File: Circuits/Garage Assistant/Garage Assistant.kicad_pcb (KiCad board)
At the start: 2 copper layers, 80.8 x 56.9 mm, 45 parts, among them P1 MOTION_A, P2 MOTION_B, P3 AC_IN, P4 3.5mm_11pin, P5 OUT_A, P6 OUT_B, Q1 TIP122, Q2 TIP122, U1 HiLink_5V3W

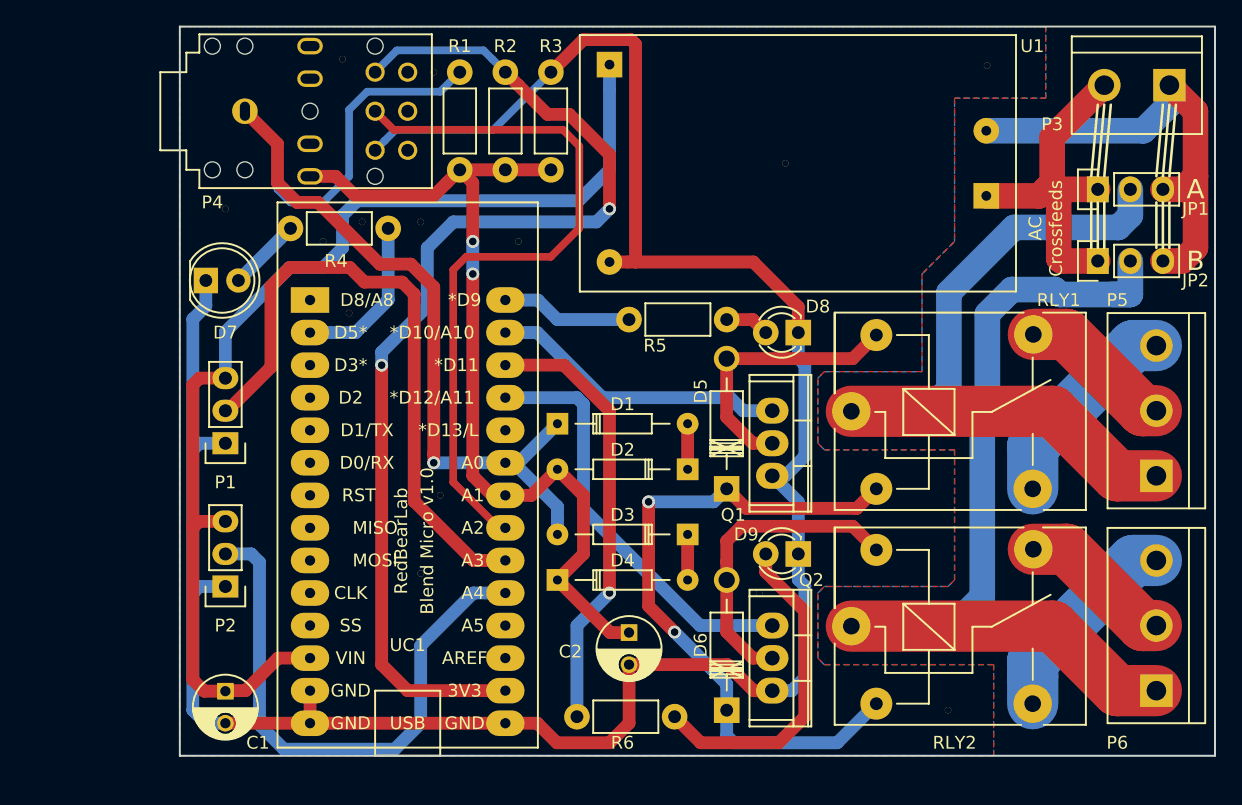
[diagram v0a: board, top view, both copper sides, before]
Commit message: Circuits: Updated 3d models on Garage Assistant
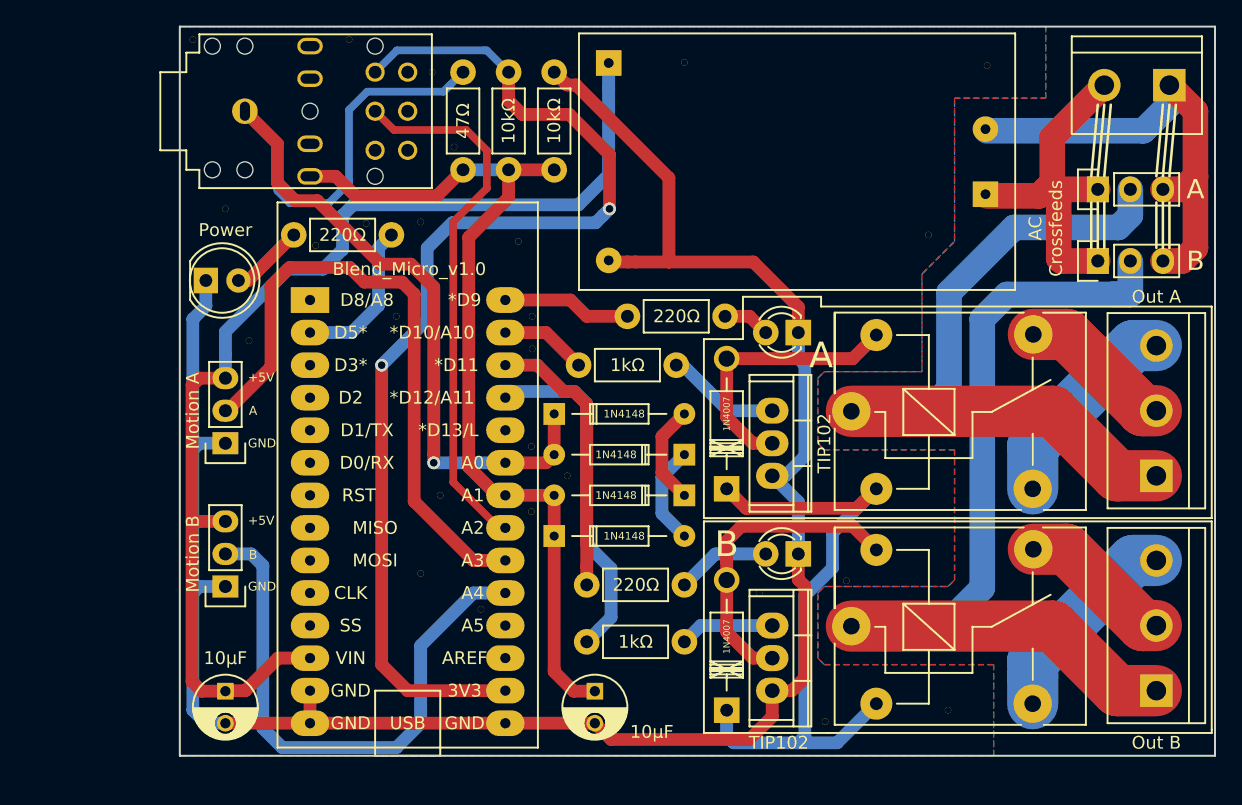
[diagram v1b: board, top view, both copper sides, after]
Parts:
- added ?: , Footprints:Thermal_Via_NoRing, F.Cu at (115.6, 89.5)
- added ?: , Footprints:Thermal_Via_NoRing, F.Cu at (111.3, 66.0)
- added ?: , Footprints:Thermal_Via_NoRing, F.Cu at (168.7, 81.3)
- added ?: , Footprints:Thermal_Via_NoRing, F.Cu at (137.7, 97.8)
- added ?: , Footprints:Thermal_Via_NoRing, F.Cu at (140.5, 100.1)
- added ?: , Footprints:Thermal_Via_NoRing, F.Cu at (131.6, 74.4)
- added ?: , Footprints:Thermal_Via_NoRing, F.Cu at (127.1, 87.6)
- added ?: , Footprints:Thermal_Via_NoRing, F.Cu at (120.8, 82.1)
- added ?: , Footprints:Thermal_Via_NoRing, F.Cu at (137.7, 102.9)
- added ?: , Footprints:Thermal_Via_NoRing, F.Cu at (137.7, 87.6)
- added ?: , Footprints:Thermal_Via_NoRing, F.Cu at (133.7, 110.5)
- added ?: , Footprints:Thermal_Via_NoRing, F.Cu at (160.6, 119.3)
- added ?: , Footprints:Thermal_Via_NoRing, F.Cu at (162.2, 108.3)
- added R7: 220Ω, Resistors_ThroughHole:Resistor_Horizontal_RM7mm, F.Cu at (152.8, 87.6)
- added R8: 220Ω, Resistors_ThroughHole:Resistor_Horizontal_RM7mm, F.Cu at (149.6, 108.6)
- D5, D6: value 1N4002 -> 1N4007
- D7: value LED_PWR -> Power
- D8: value LED_A -> A
- D9: value LED_B -> B
- JP1: value CROSSFEED_A -> Crossfeed A
- JP2: value CROSSFEED_B -> Crossfeed B
- P1: value MOTION_A -> Motion A
- P2: value MOTION_B -> Motion B
- P3: value AC_IN -> AC Input
- P5: value OUT_A -> Out A
- P6: value OUT_B -> Out B
- Q1, Q2: value TIP122 -> TIP102
- R4, R5: value 220Ω -> 1kΩ
- moved R6 47.9 mm to (119.1, 81.3), turned to 0 degrees
- moved R4 31.9 mm to (149.0, 91.4), turned to 180 degrees
- moved R5 25.4 mm to (149.6, 113.0)
- moved ? 18.3 mm to (137.7, 90.2)
- moved ? 11.1 mm to (149.6, 67.8)
- moved D3 6.23 mm to (149.6, 98.4)
- moved C2 5.29 mm to (142.6, 116.9)
- moved D4 3.44 mm to (139.4, 104.8)
- moved D2 2.05 mm to (149.6, 101.6)
- moved ? 1.61 mm to (123.4, 66.0)
- moved ? 1.02 mm to (123.4, 86.4)
- moved D1 0.81 mm to (139.4, 95.2)
- moved ? 0.34 mm to (124.8, 80.4)
- moved R1 0.25 mm to (132.3, 68.6)
- moved R2 0.25 mm to (135.9, 68.6)
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- renumbered UC1 to MC1
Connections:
- Q1 pad 1: A_RELAY -> Net-(Q1-Pad1)
- Q2 pad 1: B_RELAY -> Net-(Q2-Pad1)
- R4 pad 1: Net-(D7-Pad2) -> Net-(Q1-Pad1)
- R4 pad 2: PWR_LED -> A_RELAY
- R5 pad 1: Net-(D8-Pad2) -> Net-(Q2-Pad1)
- R5 pad 2: A_LED -> B_RELAY
- R6 pad 1: Net-(D9-Pad2) -> Net-(D7-Pad2)
- R6 pad 2: B_LED -> PWR_LED
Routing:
- net GND: track 186.3 -> 161.6 mm
- net Net-(D9-Pad2): track 25.8 -> 7.35 mm
- net A_RELAY: track 23.4 -> 6.77 mm
- net CS_CONNECT: track 56.8 -> 42.5 mm
- net B_LED: track 34.5 -> 21.7 mm, vias 1 -> 0
- net Net-(Q1-Pad1): track 0.00 -> 8.97 mm
- net Net-(Q2-Pad1): track 0.00 -> 7.38 mm
- net B_RELAY: track 33.0 -> 27.1 mm
- net Net-(D1-Pad2): track 3.56 -> 7.80 mm
- net Net-(D3-Pad1): track 3.56 -> 7.80 mm
- net SENSE: track 83.5 -> 80.1 mm
- net +5VDC: track 53.4 -> 50.4 mm, vias 2 -> 0
- net 3V3: track 86.6 -> 87.9 mm
- net /B_COMMON: track 75.4 -> 74.7 mm
- net PWR_LED: track 12.7 -> 12.1 mm
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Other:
- net class Thin added: clearance 0.4, trace_width 0.6, via_dia 0.6, via_drill 0.4
- board text added: "+5V"
- board text added: "C"
- board text added: "GND"
- board text added: "NC"
- board text added: "NO"
- board text added: "OUT A"
- board text added: "OUT B"

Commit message: Garage Assistant: Updating
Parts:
- added C3: 100µF, Capacitors_ThroughHole:CP_Radial_D6.3mm_P2.50mm, F.Cu at (148.8, 118.2)
- added D10: B, LEDs:LED_D3.0mm, F.Cu at (112.4, 90.0)
- D5: value 1N4007 -> LED_PWR; footprint Diodes_ThroughHole:Diode_DO-41_SOD81_Horizontal_RM10 -> LEDs:LED_D5.0mm
- D7: value Power -> 1N4007; footprint LEDs:LED-5MM -> LEDs:LED_D5.0mm
- D8: value A -> LED_OPT; footprint LEDs:LED-3MM -> LEDs:LED_D3.0mm
- D9: value B -> A
- JP1: value Crossfeed A -> CROSSFEED_A
- JP2: value Crossfeed B -> CROSSFEED_B
- P1: value Motion A -> MOTION_A
- P2: value Motion B -> MOTION_B
- P3: value AC Input -> AC_IN
- P5: value Out A -> OUT_A
- P6: value Out B -> OUT_B
- R4: value 1kΩ -> 220Ω
- R6: value 220Ω -> 1kΩ
- moved D5 51.3 mm to (103.2, 88.6)
- moved ? 7.12 mm to (108.5, 89.2)
- moved ? 4.34 mm to (109.5, 79.7)
- moved P1 2.29 mm to (113.8, 99.8)
- moved D7 1.98 mm to (112.5, 82.9)
- moved P2 1.40 mm to (113.8, 110.1)
- moved C2 1.27 mm to (141.4, 116.9)
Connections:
- D5 pad 1: +5VDC -> GND
- D6 pad 1: +5VDC -> +5V
- D7 pad 1: GND -> +5V
- P4 pad 6: 3V3 -> +3V3
- Q1 pad 2: Net-(D5-Pad2) -> Net-(D6-Pad2)
- Q2 pad 2: Net-(D6-Pad2) -> Net-(D7-Pad2)
- R2 pad 1: 3V3 -> +3V3
- R4 pad 1: Net-(Q1-Pad1) -> Net-(D5-Pad2)
- R4 pad 2: A_RELAY -> PWR_LED
- R5 pad 1: Net-(Q2-Pad1) -> Net-(Q1-Pad1)
- R5 pad 2: B_RELAY -> A_RELAY
- R6 pad 1: Net-(D7-Pad2) -> Net-(Q2-Pad1)
- R6 pad 2: PWR_LED -> B_RELAY
- R7 pad 2: A_LED -> OPT_LED
- R8 pad 2: B_LED -> A_LED
- RLY1 pad 1: Net-(D5-Pad2) -> Net-(D6-Pad2)
- RLY1 pad 2: +5VDC -> +5V
- RLY2 pad 1: Net-(D6-Pad2) -> Net-(D7-Pad2)
- RLY2 pad 2: +5VDC -> +5V
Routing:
- net +5VDC: track 50.4 -> 0.00 mm
- net GND: track 161.6 -> 122.0 mm
- net +5V: track 88.0 -> 120.0 mm
- net 3V3: track 87.9 -> 59.3 mm, vias 2 -> 1
- net +3V3: track 0.00 -> 28.6 mm, vias 0 -> 1
- net A_LED: track 10.1 -> 34.7 mm
- net A_RELAY: track 6.77 -> 24.7 mm
- net Net-(D6-Pad2): track 24.4 -> 41.7 mm
- net Net-(D5-Pad2): track 21.4 -> 5.54 mm
- net Net-(UC1-Pad3): track 0.00 -> 12.1 mm
- net B_RELAY: track 27.1 -> 15.2 mm
- net PWR_LED: track 12.1 -> 6.09 mm
- net Net-(Q1-Pad1): track 8.97 -> 5.23 mm
- net OPT_LED: track 0.00 -> 3.18 mm
- net A_MOTION: track 49.1 -> 46.1 mm
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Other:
- board text added: "OPT"
- board text added: "PWR"
